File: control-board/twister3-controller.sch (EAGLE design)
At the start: 58 parts, among them J1 BARREL-JACK_PJ-063BH, J5 OSTVN04A150, U1 IS31FL3193, U2 MIC4680-5.0YM-TR, U3 MAX6816, U4 TMC2130-LA, U5 Teensy 3.2, U6 GDM1602K

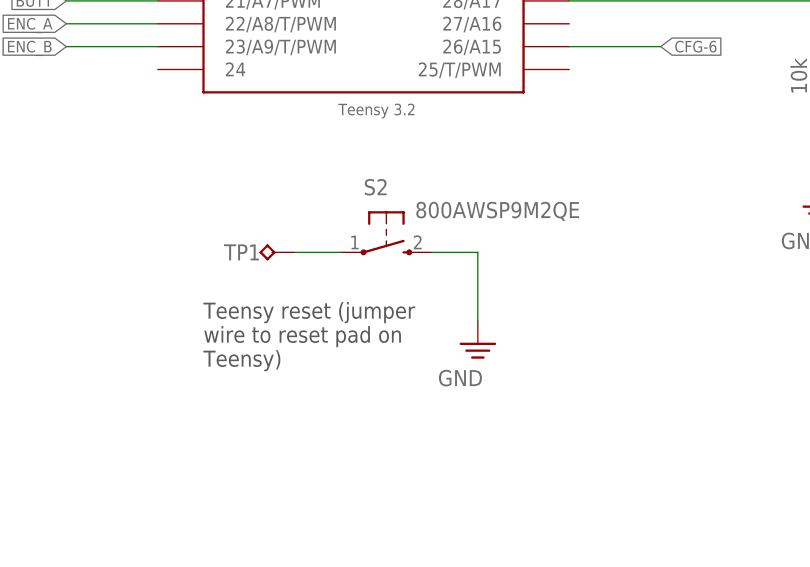
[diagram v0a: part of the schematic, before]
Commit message: Removed trimpot access in control board front panel
- Trimpots should be set during assembly and glued, access is not
required during operaiton. Also, current trimpot only works if the
silent stepper stick module is not used with is not the default case.
- Also, removed reset switch (since this can be done by removing
power...)
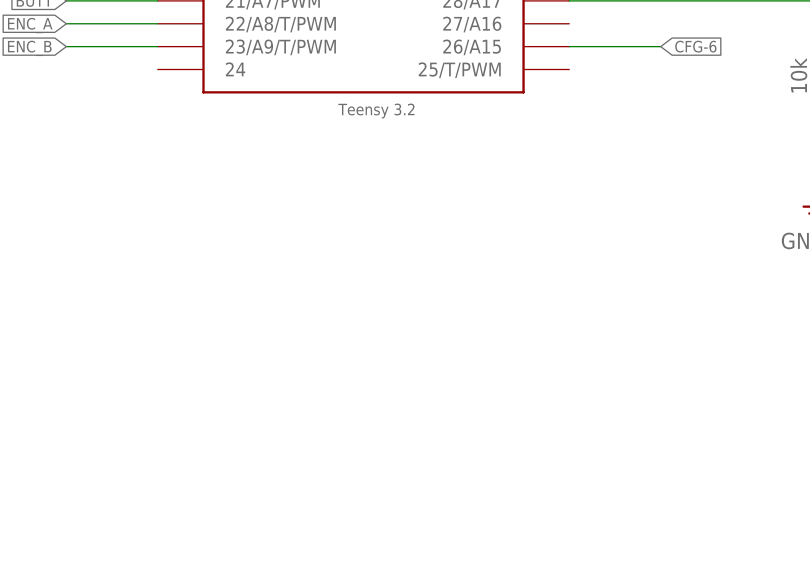
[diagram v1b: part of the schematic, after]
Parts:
- removed S2: 800AWSP9M2QE, jonnew:SPST_TACT2_800AW
- removed TP1: RESET, jonnew:TP_1MM
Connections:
- removed net N$23: S2.P, TP1.TP
- net GND: no longer S2.S
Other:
- note removed: "Teensy reset (jumper wire to reset pad on Teensy)"
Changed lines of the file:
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@@
 <part name="SUPPLY32" library="jonnew" deviceset="GND" device=""/>
 <part name="SUPPLY33" library="jonnew" deviceset="GND" device=""/>
-<part name="S2" library="jonnew" deviceset="SPST_TACT2" device="_800AW" value="800AWSP9M2QE"/>
-<part name="TP1" library="jonnew" deviceset="TP" device="_1MM" value="RESET"/>
-<part name="SUPPLY34" library="jonnew" deviceset="GND" device=""/>
 <part name="R12" library="cyclops" deviceset="R" device="_0603" value="4.7k"/>
 <part name="R11" library="cyclops" deviceset="R" device="_0603" value="4.7k"/>
@@
 <text x="121.92" y="226.06" size="1.27" layer="97" rot="R90">NB: Override internal pullup</text>
 <frame x1="0" y1="0" x2="551.18" y2="335.28" columns="8" rows="5" layer="94"/>
-<text x="165.1" y="43.18" size="1.778" layer="97">Teensy reset (jumper
-wire to reset pad on
-Teensy)</text>
 <text x="353.06" y="50.8" size="1.778" layer="97">Mechanical connections
 between panel and board.</text>
@@
 <instance part="SUPPLY32" gate="PE" x="233.68" y="60.96"/>
 <instance part="SUPPLY33" gate="PE" x="487.68" y="86.36"/>
-<instance part="S2" gate="G$1" x="185.42" y="55.88" rot="R270"/>
-<instance part="TP1" gate="G$1" x="172.72" y="55.88" rot="R90"/>
-<instance part="SUPPLY34" gate="PE" x="195.58" y="45.72"/>
 <instance part="R12" gate="R" x="259.08" y="96.52" rot="R90"/>
 <instance part="R11" gate="R" x="251.46" y="96.52" rot="R90"/>
@@
 </segment>
 <segment>
-<pinref part="S2" gate="G$1" pin="S"/>
-<wire x1="190.5" y1="55.88" x2="195.58" y2="55.88" width="0.1524" layer="91"/>
-<wire x1="195.58" y1="55.88" x2="195.58" y2="48.26" width="0.1524" layer="91"/>
-<pinref part="SUPPLY34" gate="PE" pin="GND"/>
-</segment>
-<segment>
 <pinref part="R17" gate="R" pin="2"/>
 <wire x1="233.68" y1="68.58" x2="233.68" y2="63.5" width="0.1524" layer="91"/>
@@
 </segment>
 </net>
-<net name="N$23" class="0">
-<segment>
-<pinref part="TP1" gate="G$1" pin="TP"/>
-<pinref part="S2" gate="G$1" pin="P"/>
-<wire x1="175.26" y1="55.88" x2="180.34" y2="55.88" width="0.1524" layer="91"/>
-</segment>
-</net>

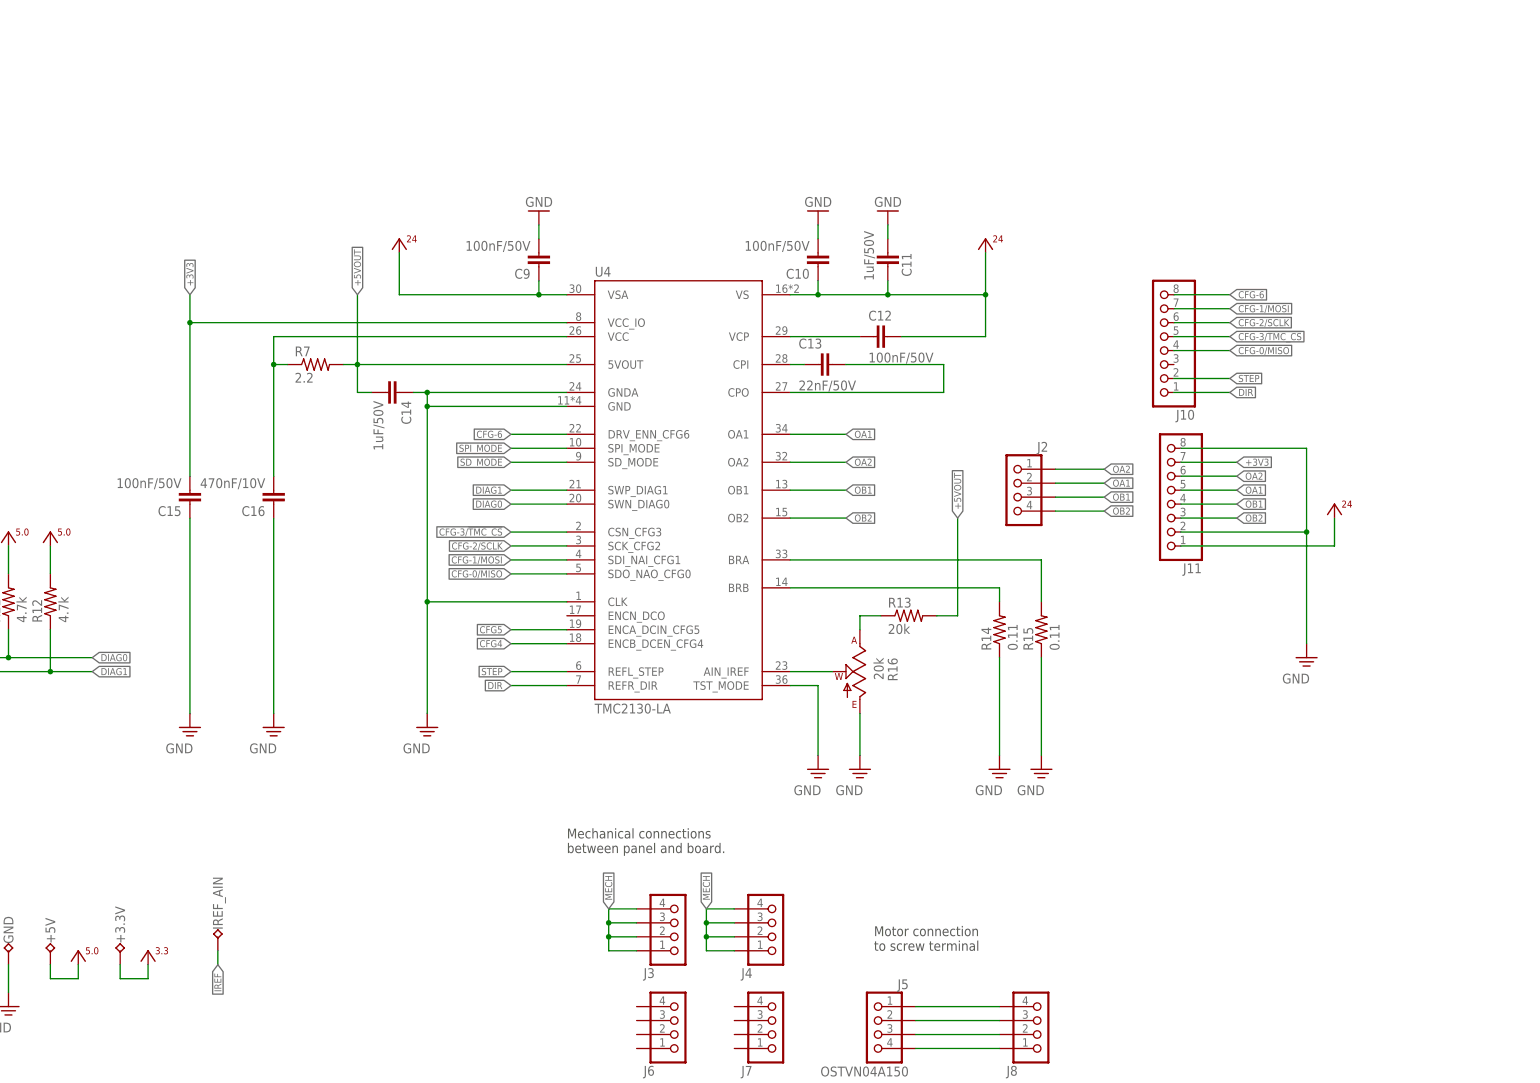
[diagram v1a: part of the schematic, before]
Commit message: Some minor updates to MANUAL.*
- Also updated control board schematic to indicate that stepper driver
circuit should not be populated if you are using a silent stepper stick.
- At this point, I'm considering the MANUAL deprecated and moving its
contents to the paper, which will act as a manual when it is finished.
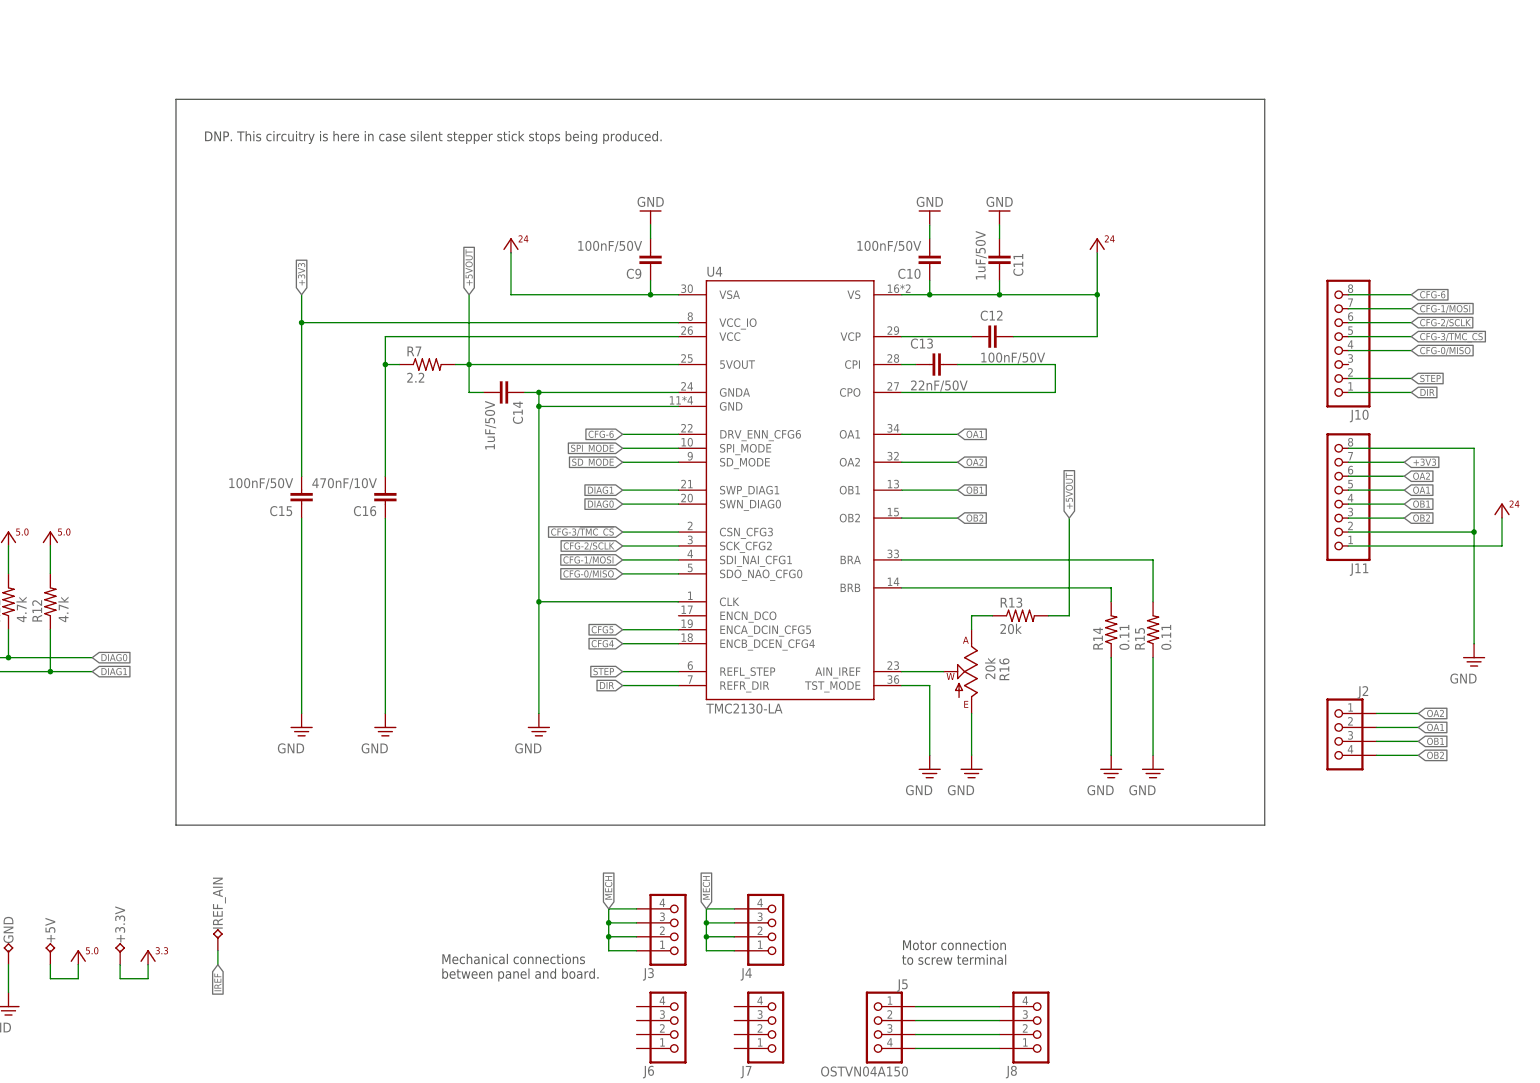
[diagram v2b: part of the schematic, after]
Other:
- note added: "DNP. This circuitry is here in case silent stepper stick stops being produced."
- moved on the sheet: C10, C11, C12, C13, C14, C15, C16, C9, J10, J11, J2, R13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

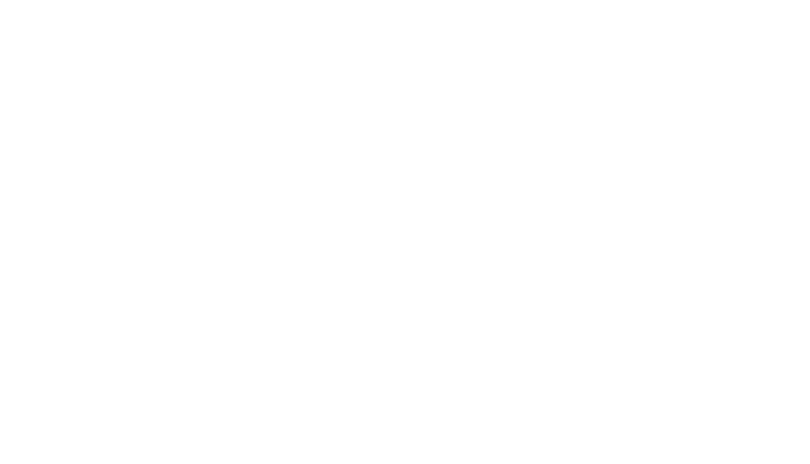
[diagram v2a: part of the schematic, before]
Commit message: Added oe-logo and Twister 3 to tstop on front panel
- Reduced the both bcream and bstop for the SMD threaded inserts to 3.2
mm on bottom on front panel
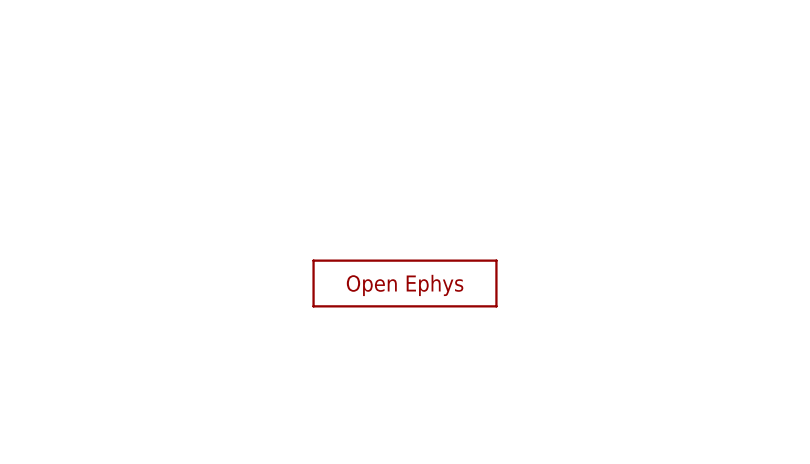
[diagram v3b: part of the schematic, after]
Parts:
- added X1: OE-LOGO_14X10, jonnew:OE-LOGO_14X10
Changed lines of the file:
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@@
 <part name="P+3" library="jonnew" deviceset="+5V" device=""/>
 <part name="SUPPLY27" library="jonnew" deviceset="+3V3" device=""/>
+<part name="X1" library="jonnew" deviceset="OE-LOGO" device="_14X10"/>
 </parts>
 <sheets>
@@
 <instance part="P+3" gate="1" x="264.16" y="33.02"/>
 <instance part="SUPPLY27" gate="PWR1" x="276.86" y="30.48"/>
+<instance part="X1" gate="G$1" x="172.72" y="25.4"/>
 </instances>
 <busses>

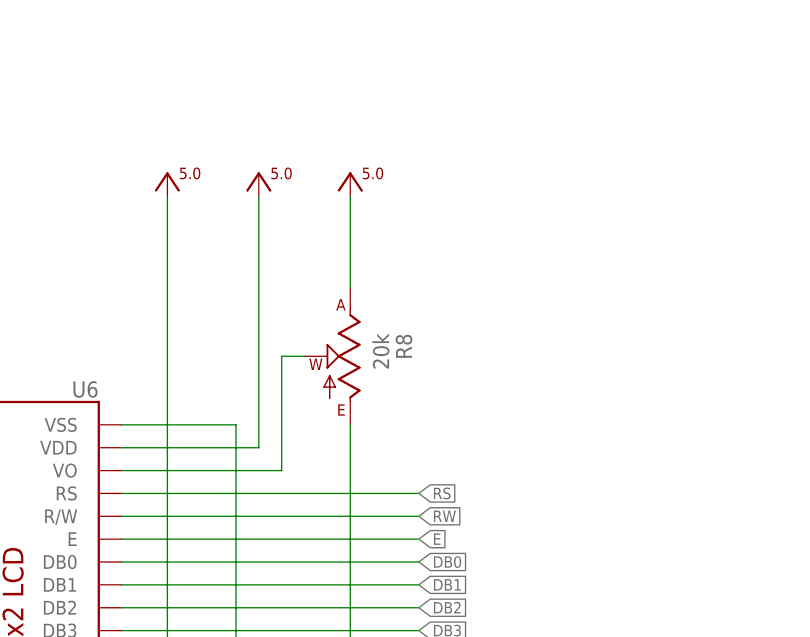
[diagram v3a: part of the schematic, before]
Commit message: Move potentiometers to bottom of board
- This will cut down on production costs since they are not available
through the front panel anyway
- Alternative, hard-coded resistor (not populated) for LCD bias
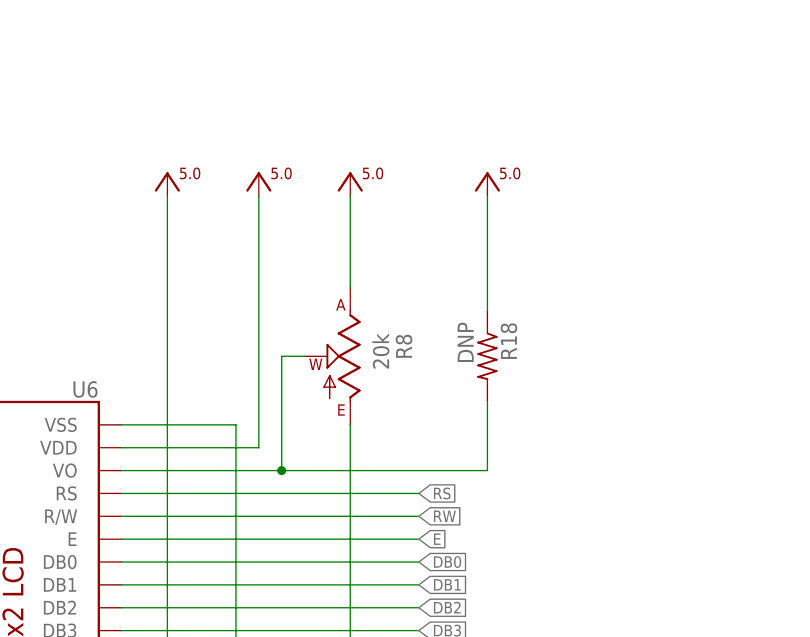
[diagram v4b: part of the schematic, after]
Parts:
- added R18: DNP, jonnew:R_0603
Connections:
- net +5V0: now also R18.1
- net N$11: now also R18.2
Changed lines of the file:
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@@
 <setting verticaltext="up"/>
 </settings>
-<grid distance="0.1" unitdist="inch" unit="inch" style="lines" multiple="1" display="yes" altdistance="0.01" altunitdist="inch" altunit="inch"/>
+<grid distance="0.1" unitdist="inch" unit="inch" style="lines" multiple="1" display="no" altdistance="0.01" altunitdist="inch" altunit="inch"/>
 <layers>
 <layer number="1" name="Top" color="4" fill="1" visible="no" active="no"/>
@@
 <part name="SUPPLY27" library="jonnew" deviceset="+3V3" device=""/>
 <part name="X1" library="jonnew" deviceset="OE-LOGO" device="_14X10"/>
+<part name="R18" library="jonnew" deviceset="R" device="_0603" value="DNP"/>
+<part name="P+13" library="jonnew" deviceset="+5V" device=""/>
 </parts>
 <sheets>
@@
 <instance part="SUPPLY27" gate="PWR1" x="276.86" y="30.48"/>
 <instance part="X1" gate="G$1" x="172.72" y="25.4"/>
+<instance part="R18" gate="R" x="78.74" y="132.08" rot="R270"/>
+<instance part="P+13" gate="1" x="78.74" y="152.4"/>
 </instances>
 <busses>
@@
 <wire x1="55.88" y1="119.38" x2="55.88" y2="132.08" width="0.1524" layer="91"/>
 <wire x1="55.88" y1="132.08" x2="58.42" y2="132.08" width="0.1524" layer="91"/>
+<pinref part="R18" gate="R" pin="2"/>
+<wire x1="55.88" y1="119.38" x2="78.74" y2="119.38" width="0.1524" layer="91"/>
+<wire x1="78.74" y1="119.38" x2="78.74" y2="127" width="0.1524" layer="91"/>
+<junction x="55.88" y="119.38"/>
 </segment>
 </net>
@@
 <pinref part="P+3" gate="1" pin="+5V0"/>
 </segment>
-</net>
+<segment>
+<pinref part="R18" gate="R" pin="1"/>
+<pinref part="P+13" gate="1" pin="+5V0"/>
+<wire x1="78.74" y1="137.16" x2="78.74" y2="149.86" width="0.1524" layer="91"/>
+</segment>
+</net>
